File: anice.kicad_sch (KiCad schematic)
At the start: 8 parts, among them J1 Conn_02x20_Counter_Clockwise, J2 Micro_SD_Card_Det1, U1 ECP5U_12_CABGA256, Y1 ECS-2520MV-xxx-xx

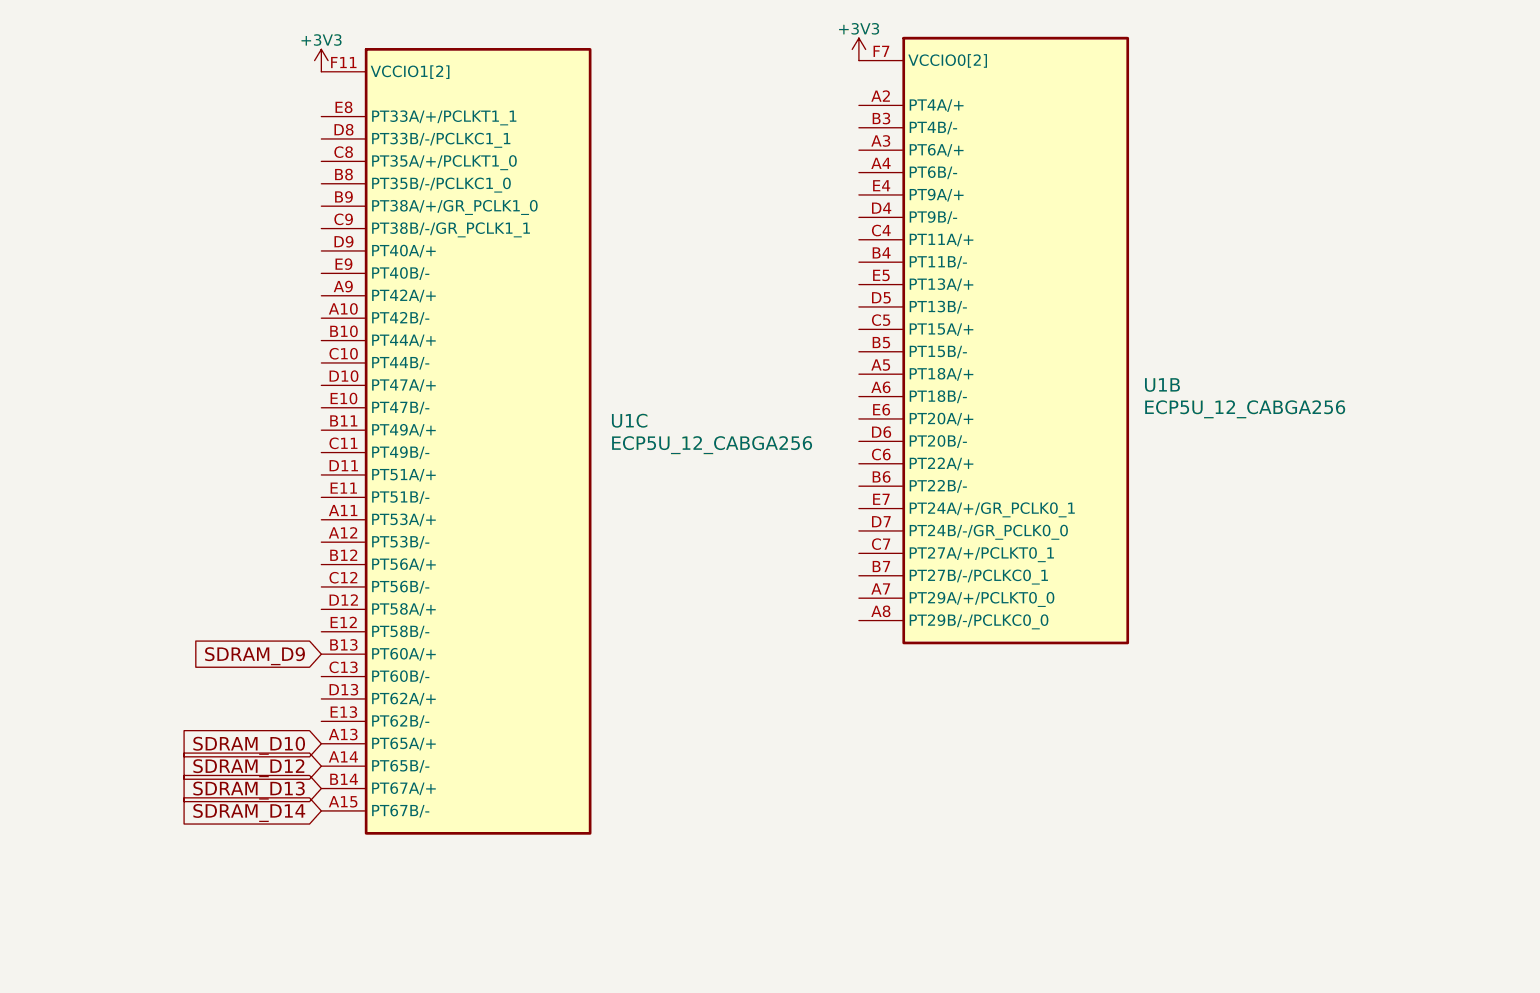
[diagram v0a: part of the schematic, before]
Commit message: Routed HDMI, usb, rotated chip and more
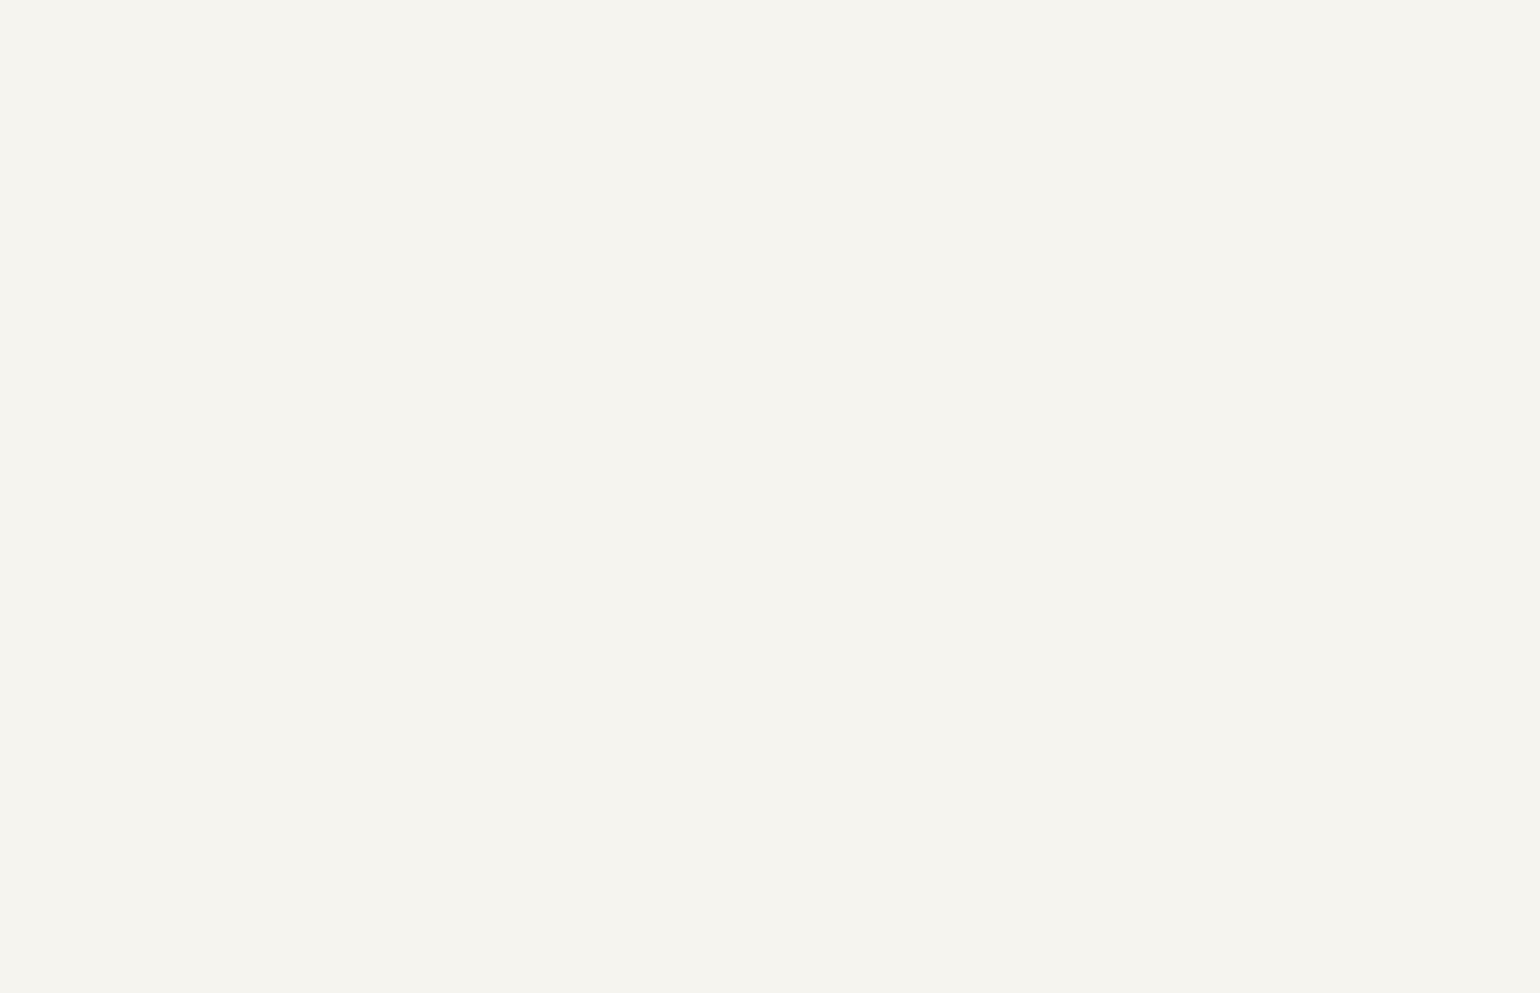
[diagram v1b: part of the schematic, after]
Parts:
- removed U1: ECP5U_12_CABGA256, Package_BGA:BGA-256_14.0x14.0mm_Layout16x16_P0.8mm_Ball0.45mm_Pad0.32mm_NSMD, symbol josh-ic:ECP5U_12_CABGA256

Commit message: Stash
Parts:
- removed Y1: ECS-2520MV-xxx-xx, Crystal:Crystal_SMD_3225-4Pin_3.2x2.5mm, symbol Oscillator:ECS-2520MV-xxx-xx
- added U1: ECP5U_12_CABGA256, Package_BGA:BGA-256_14.0x14.0mm_Layout16x16_P0.8mm_Ball0.45mm_Pad0.32mm_NSMD, symbol josh-ic:ECP5U_12_CABGA256
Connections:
- net +3V3: now also U1.J6 (VCCIO6[2]), U1.J7 (VCCIO6[2])
- net CONN10: now reaches J1.10 (Pin_10)
- net CONN11: now reaches J1.11 (Pin_11)
- net CONN12: now reaches J1.12 (Pin_12)
- net CONN13: now reaches J1.13 (Pin_13)
- net CONN15: now reaches J1.15 (Pin_15)
- net CONN15: now also U1.R1 (PL35B/-/VREF1_6/HS/LDQ32)
- net CONN16: now reaches J1.16 (Pin_16)
- net CONN18: now reaches J1.18 (Pin_18)
- net CONN19: now reaches J1.19 (Pin_19)
- net CONN21: now reaches J1.21 (Pin_21)
- net CONN22: now reaches J1.22 (Pin_22)
- net CONN23: now reaches J1.23 (Pin_23)
- net CONN24: now reaches J1.24 (Pin_24)
- net CONN26: now reaches J1.26 (Pin_26)
- net CONN27: now reaches J1.27 (Pin_27)
- net CONN28: now reaches J1.28 (Pin_28)
- net CONN29: now reaches J1.29 (Pin_29)
- net CONN3: now reaches J1.3 (Pin_3)
- net CONN3: now also U1.T3 (PL41D/-/LDQ44)
- net CONN31: now reaches J1.31 (Pin_31)
- net CONN32: now reaches J1.32 (Pin_32)
- net CONN33: now reaches J1.33 (Pin_33)
- net CONN35: now reaches J1.35 (Pin_35)
- net CONN36: now reaches J1.36 (Pin_36)
- net CONN37: now reaches J1.37 (Pin_37)
- net CONN38: now reaches J1.38 (Pin_38)
- net CONN40: now reaches J1.40 (Pin_40)
- net CONN5: now reaches J1.5 (Pin_5)
- net CONN5: now also U1.R3 (PL41B/-/HS/LDQ44)
- net CONN7: now reaches J1.7 (Pin_7)
- net CONN7: now also U1.T2 (PL38D/-/LDQ44)
- net CONN8: now reaches J1.8 (Pin_8)
- net CONN8: now also U1.R2 (PL38C/+/LDQ44)
- new net FPDI_SCL: U1.R4 (PL41C/+/LDQ44)
- new net FPDI_SDA: U1.P5 (PL47D/-/LLC_GPLL0C_IN/LDQ44)
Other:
- moved on the sheet: J1

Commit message: Rev 1
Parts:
- removed J2: Micro_SD_Card_Det1, anice-lib:SDCard molex, symbol Connector:Micro_SD_Card_Det2
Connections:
- net CONN10: now also U1.P2 (PL32B/-/HS/LDQSN32)
- net CONN11: now also U1.M3 (PL32D/-/LDQ32)
- net CONN12: now also U1.P1 (PL35A/+/HS/LDQ32)
- net CONN13: now also U1.L3 (PL32C/+/LDQ32)
- net CONN16: now also U1.P3 (PL38B/-/HS/LDQ44)
- net CONN18: now also U1.N1 (PL32A/+/HS/LDQS32)
- net CONN19: now also U1.M2 (PL26D/-/PCLKC6_0/LDQ32)
- net CONN21: now also U1.L1 (PL26A/+/PCLKT6_1/HS/LDQ32)
- net CONN22: now also U1.M1 (PL26C/+/PCLKT6_0/LDQ32)
- net CONN24: now also U1.L2 (PL26B/-/PCLKC6_1/HS/LDQ32)
- net SD_CLK: now reaches U1.L4 (PL29C/+/GR_PCLK6_1/LDQ32)
- net SD_D2: now reaches U1.N4 (PL38A/+/HS/LDQ44)
- net SD_D3: now reaches U1.P4 (PL41A/+/HS/LDQ44)
- net SD_D0: now reaches U1.T4 (PL44B/-/HS/LDQSN44)
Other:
- moved on the sheet: J1, U1F

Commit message: No DRC Errors
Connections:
- net SD_CMD: now reaches U1.R5 (PL44A/+/HS/LDQS44)
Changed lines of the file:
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@@
+		)
+	)
+	(global_label "SD_CMD"
+		(shape input)
+		(at 137.16 88.9 0)
+		(fields_autoplaced yes)
+		(effects
+			(font
+				(size 1.27 1.27)
+			)
+			(justify left)
+		)
+		(property "Intersheetrefs" "${INTERSHEET_REFS}"
+			(at 147.5837 88.9 0)
+			(effects
+				(font
+					(size 1.27 1.27)
+				)
+				(justify left)
+				(hide yes)
+			)
 		)
 	)
